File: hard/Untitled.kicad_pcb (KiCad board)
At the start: 2 copper layers, 99.6 x 75.1 mm, 93 parts, among them IC2 MTCH6102-I_SS, J2 USB_C_Receptacle, J3 Black headphone jack, J5 TP1, J7 TP3, SW1 RotaryEncoder_Switch, SW90 BOOT, SW91 RESET, U1 RP2040, U10 TLV9062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

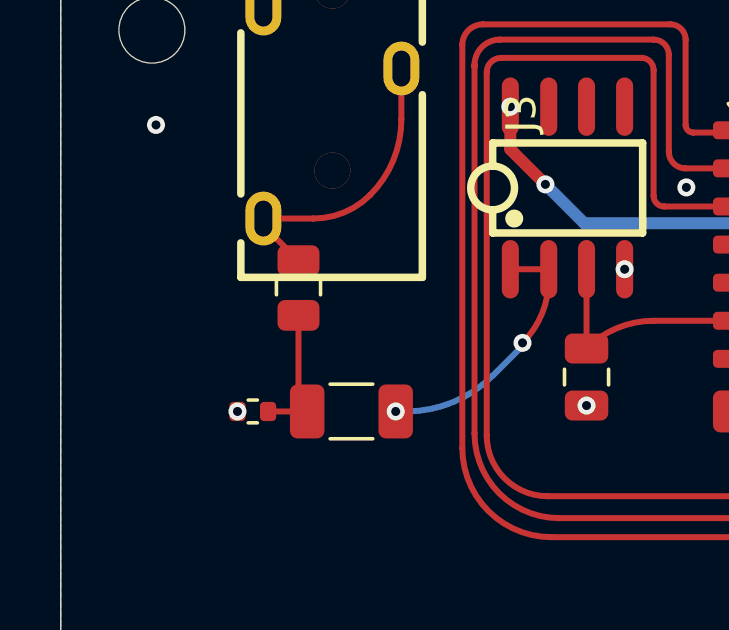
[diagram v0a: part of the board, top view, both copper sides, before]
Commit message: fixed position of jack
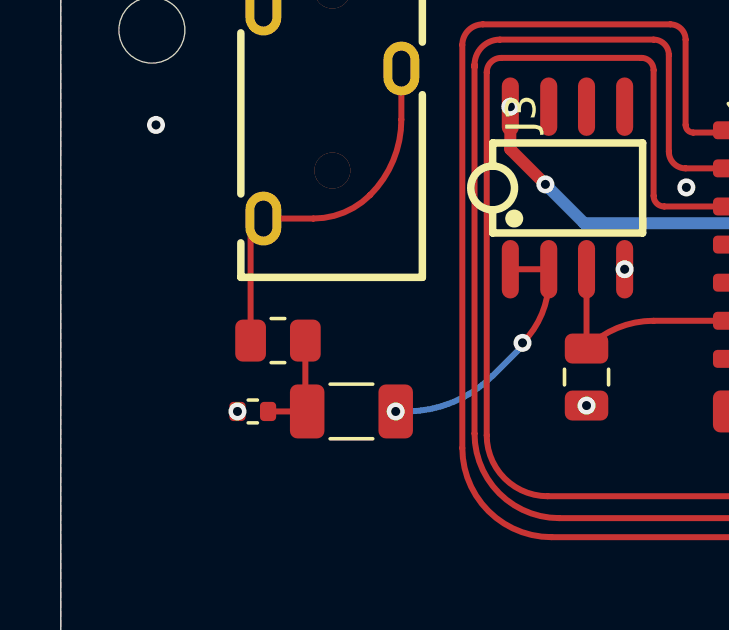
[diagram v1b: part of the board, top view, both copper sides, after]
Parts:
- moved R20 1.88 mm to (93.7, 61.8), turned to 180 degrees
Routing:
- net Net-(J3-L): track 10.1 -> 12.9 mm
- net Net-(C46-Pad1): track 4.98 -> 4.46 mm

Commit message: fixed pad errors
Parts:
- R4, R5: footprint Resistor_SMD:R_0201_0603Metric -> Resistor_SMD:R_0402_1005Metric
- U6: footprint Package_SON:WSON-8-1EP_6x5mm_P1.27mm_EP3.4x4.3mm -> Package_SO:SOIC-8_5.3x5.3mm_P1.27mm
- moved U6 0.86 mm to (174.2, 77.3)
- moved C29 0.74 mm to (171.2, 67.7)
- moved C50 0.74 mm to (173.7, 67.7)
- moved R15 0.74 mm to (170.0, 70.4)
- moved R16 0.74 mm to (172.4, 70.4)
- moved R17 0.74 mm to (175.0, 70.4)
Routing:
- net QSPI_SS_1: track 25.1 -> 29.1 mm
- net QSPI_SD2_1: track 18.7 -> 16.6 mm
- net QSPI_SD1_1: track 19.8 -> 21.3 mm
- net Net-(U1-GPIO13): track 53.5 -> 52.2 mm
- net +3V3D: track 250.4 -> 251.6 mm
- net Net-(U1-GPIO11): track 47.0 -> 45.9 mm
- net GND: track 47.7 -> 48.8 mm
- net Net-(U1-GPIO10): track 44.1 -> 45.2 mm
- net QSPI_SD0_1: track 9.79 -> 9.14 mm
- net QSPI_SD3_1: track 11.1 -> 10.6 mm
- net QSPI_SCLK_1: track 10.1 -> 9.53 mm
